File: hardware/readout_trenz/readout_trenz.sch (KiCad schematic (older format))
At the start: 1 part, among them J1 Conn_02x05_Odd_Even

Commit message: Layout Started
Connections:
- net labels removed: 1v8_GPIO1, 1v8_GPIO2, 1v8_GPIO3, 1v8_GPIO4, 3v3_GPIO1, 3v3_GPIO2, 3v3_GPIO3, 3v3_GPIO4, LVDS_GPIO_n1, LVDS_GPIO_n2, LVDS_GPIO_p1, LVDS_GPIO_p2
- wire segments 35 -> 23
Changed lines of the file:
@@
 Text Label 2550 4500 0    50   ~ 0
 B2_[0..31]
-Text Label 11550 5250 0    50   ~ 0
-LVDS_GPIO_n2
-Wire Wire Line
-	12100 5150 11550 5150
-Wire Wire Line
-	11550 5250 12100 5250
-Wire Wire Line
-	12100 4650 11650 4650
-Wire Wire Line
-	11650 4550 12100 4550
-Text Label 11650 4650 0    50   ~ 0
-3v3_GPIO2
-Text Label 11650 4550 0    50   ~ 0
-3v3_GPIO1
-Wire Wire Line
-	12100 4850 11650 4850
-Wire Wire Line
-	11650 4750 12100 4750
-Text Label 11650 4850 0    50   ~ 0
-3v3_GPIO4
-Text Label 11650 4750 0    50   ~ 0
-3v3_GPIO3
-Text Label 11550 5150 0    50   ~ 0
-LVDS_GPIO_p2
-Wire Wire Line
-	11550 5050 12100 5050
-Wire Wire Line
-	12100 4950 11550 4950
-Text Label 11550 5050 0    50   ~ 0
-LVDS_GPIO_n1
-Text Label 11550 4950 0    50   ~ 0
-LVDS_GPIO_p1
-Wire Wire Line
-	12100 4250 11650 4250
-Wire Wire Line
-	11650 4150 12100 4150
-Text Label 11650 4250 0    50   ~ 0
-1v8_GPIO2
-Text Label 11650 4150 0    50   ~ 0
-1v8_GPIO1
-Wire Wire Line
-	12100 4450 11650 4450
-Wire Wire Line
-	11650 4350 12100 4350
-Text Label 11650 4450 0    50   ~ 0
-1v8_GPIO4
-Text Label 11650 4350 0    50   ~ 0
-1v8_GPIO3
 Wire Wire Line
 	2500 6000 3500 6000

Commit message: Radout Layout in progress
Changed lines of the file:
@@
 Wire Bus Line
 	5500 2750 4500 2750
-Text Label 4600 2750 0    50   ~ 0
-Serial_ctrl[0..8]ONE
 Wire Bus Line
 	4500 5750 5500 5750
-Text Label 4650 5750 0    50   ~ 0
-Serial_ctrl[0..8]TWO
 $Sheet
 S 3500 1000 1000 2500

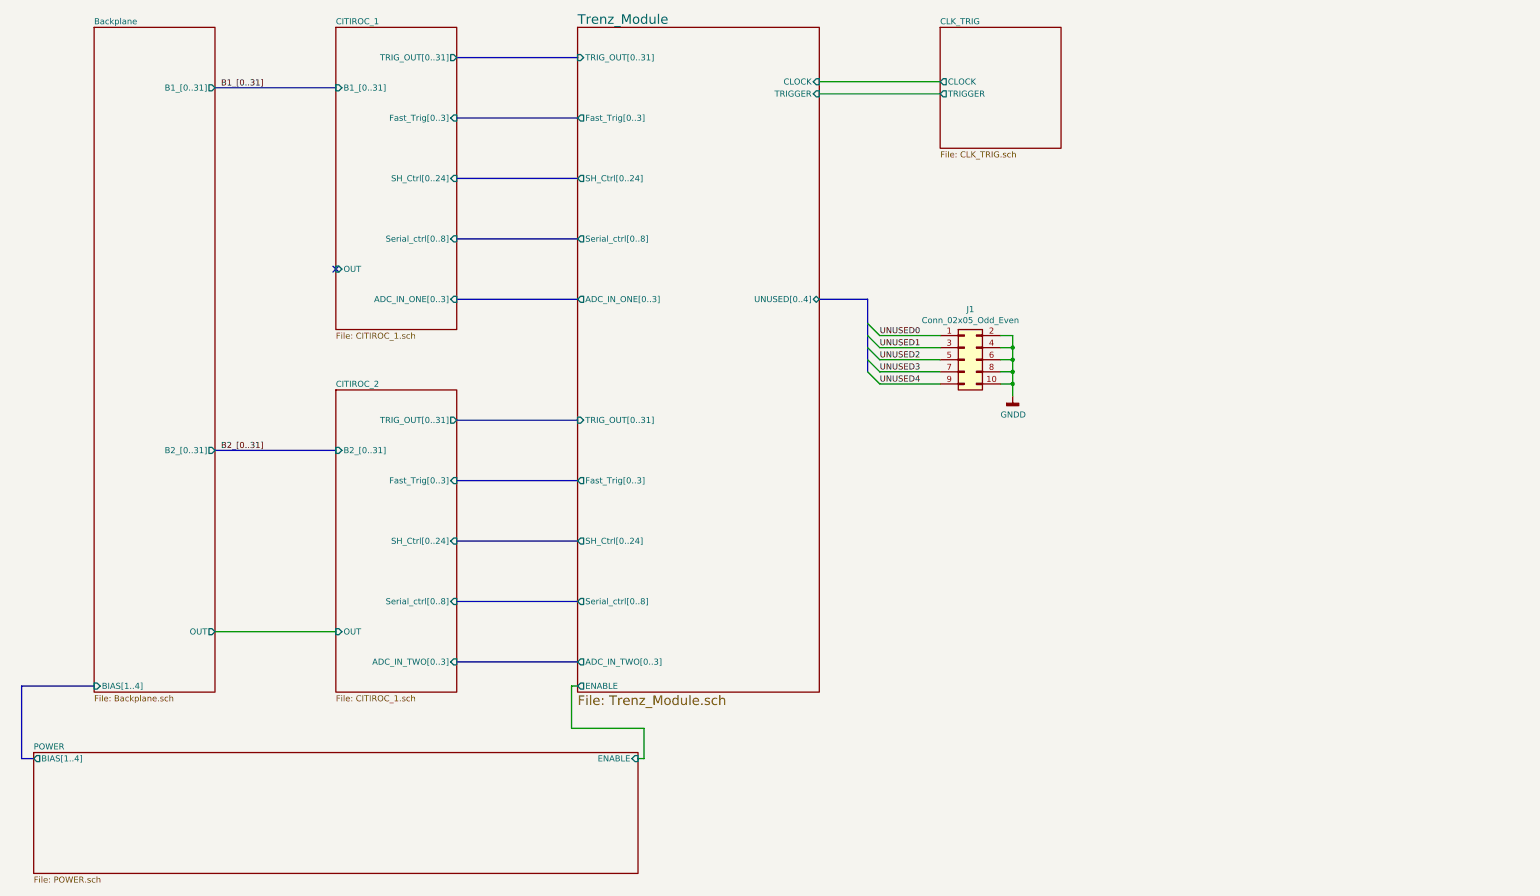
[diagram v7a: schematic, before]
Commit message: Netlist errors fixed
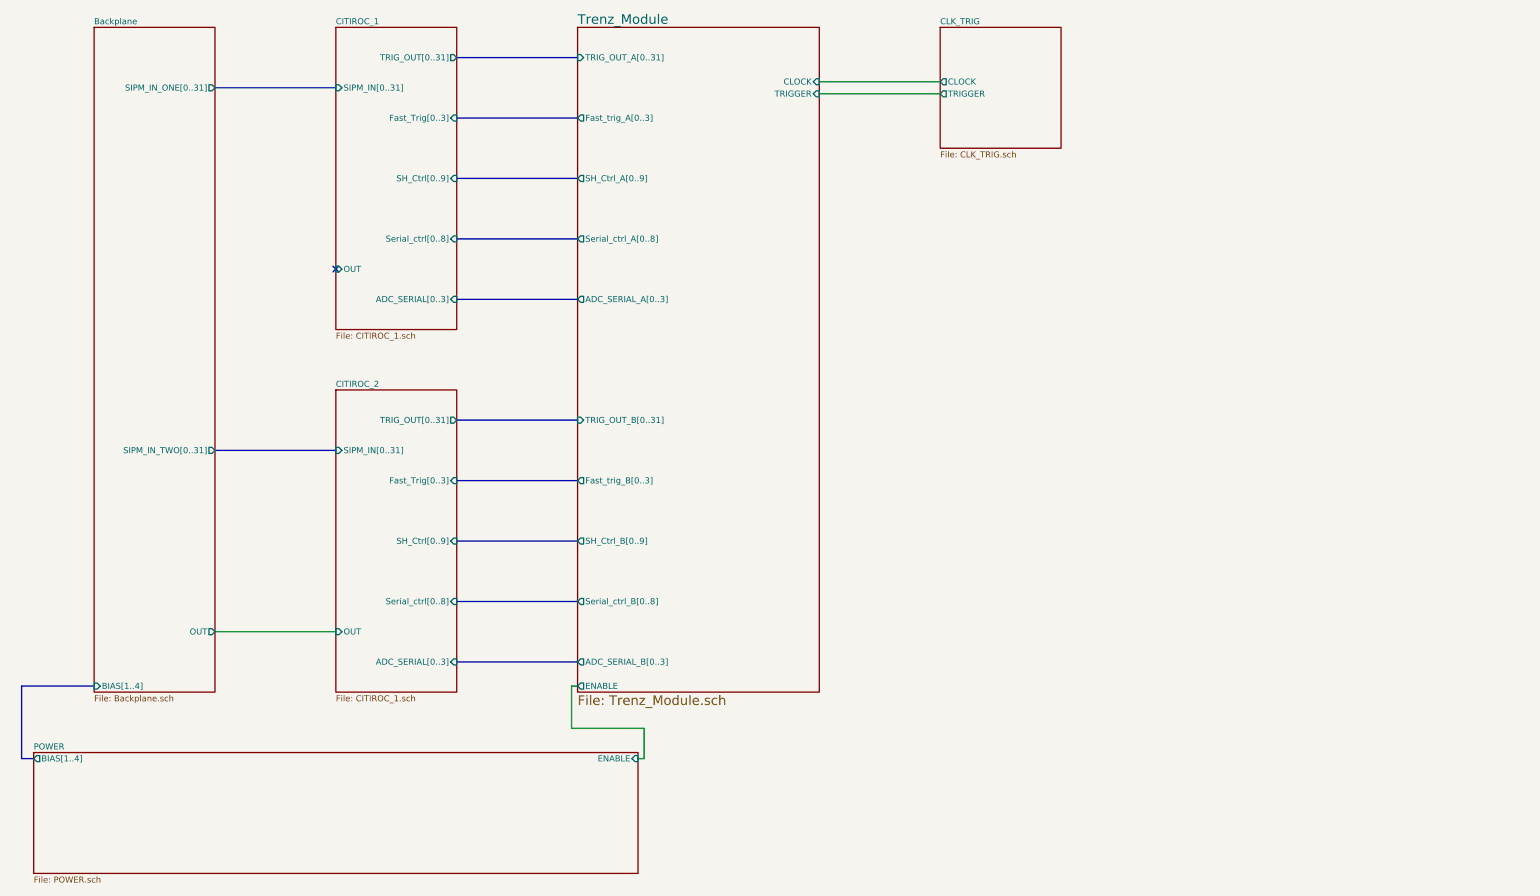
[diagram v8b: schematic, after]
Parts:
- removed J1: Conn_02x05_Odd_Even, Connector_PinHeader_2.54mm:PinHeader_2x05_P2.54mm_Vertical_SMD, symbol Connector_Generic:Conn_02x05_Odd_Even
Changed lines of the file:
@@
 Wire Bus Line
 	2500 4500 3500 4500
-Text Label 2550 4500 0    50   ~ 0
-B2_[0..31]
 Wire Wire Line
 	2500 6000 3500 6000
@@
 F0 "CITIROC_2" 50
 F1 "CITIROC_1.sch" 50
-F2 "B2_[0..31]" I L 3500 4500 50
+F2 "SIPM_IN[0..31]" I L 3500 4500 50
 F3 "OUT" I L 3500 6000 50
 F4 "TRIG_OUT[0..31]" O R 4500 4250 50
-F5 "ADC_IN_TWO[0..3]" I R 4500 6250 50
-F6 "SH_Ctrl[0..24]" I R 4500 5250 50
+F5 "ADC_SERIAL[0..3]" I R 4500 6250 50
+F6 "SH_Ctrl[0..9]" I R 4500 5250 50
 F7 "Serial_ctrl[0..8]" I R 4500 5750 50
 F8 "Fast_Trig[0..3]" I R 4500 4750 50
 $EndSheet
-Text Label 2550 1500 0    50   ~ 0
-B1_[0..31]
 $Sheet
 S 1500 1000 1000 5500
@@
 F0 "Backplane" 50
 F1 "Backplane.sch" 50
-F2 "B2_[0..31]" O R 2500 4500 50
-F3 "OUT" O R 2500 6000 50
-F4 "B1_[0..31]" O R 2500 1500 50
-F5 "BIAS[1..4]" I L 1500 6450 50
+F2 "OUT" O R 2500 6000 50
+F3 "BIAS[1..4]" I L 1500 6450 50
+F4 "SIPM_IN_ONE[0..31]" O R 2500 1500 50
+F5 "SIPM_IN_TWO[0..31]" O R 2500 4500 50
 $EndSheet
 NoConn ~ 3500 3000
@@
 F0 "Trenz_Module" 79
 F1 "Trenz_Module.sch" 79
-F2 "TRIG_OUT[0..31]" I L 5500 1250 50
-F3 "TRIG_OUT[0..31]" I L 5500 4250 50
-F4 "ADC_IN_ONE[0..3]" O L 5500 3250 50
-F5 "ADC_IN_TWO[0..3]" O L 5500 6250 50
-F6 "SH_Ctrl[0..24]" O L 5500 2250 50
-F7 "SH_Ctrl[0..24]" O L 5500 5250 50
-F8 "CLOCK" I R 7500 1450 50
-F9 "TRIGGER" I R 7500 1550 50
-F10 "ENABLE" O L 5500 6450 50
-F11 "Serial_ctrl[0..8]" O L 5500 2750 50
-F12 "Serial_ctrl[0..8]" O L 5500 5750 50
-F13 "Fast_Trig[0..3]" O L 5500 1750 50
-F14 "Fast_Trig[0..3]" O L 5500 4750 50
-F15 "UNUSED[0..4]" B R 7500 3250 50
+F2 "CLOCK" I R 7500 1450 50
+F3 "TRIGGER" I R 7500 1550 50
+F4 "ENABLE" O L 5500 6450 50
+F5 "TRIG_OUT_A[0..31]" I L 5500 1250 50
+F6 "TRIG_OUT_B[0..31]" I L 5500 4250 50
+F7 "SH_Ctrl_B[0..9]" O L 5500 5250 50
+F8 "Fast_trig_B[0..3]" O L 5500 4750 50
+F9 "ADC_SERIAL_B[0..3]" O L 5500 6250 50
+F10 "SH_Ctrl_A[0..9]" O L 5500 2250 50
+F11 "ADC_SERIAL_A[0..3]" O L 5500 3250 50
+F12 "Serial_ctrl_B[0..8]" O L 5500 5750 50
+F13 "Serial_ctrl_A[0..8]" O L 5500 2750 50
+F14 "Fast_trig_A[0..3]" O L 5500 1750 50
 $EndSheet
 Wire Wire Line
@@
 F0 "CITIROC_1" 50
 F1 "CITIROC_1.sch" 50
-F2 "B1_[0..31]" I L 3500 1500 50
+F2 "SIPM_IN[0..31]" I L 3500 1500 50
 F3 "TRIG_OUT[0..31]" O R 4500 1250 50
-F4 "ADC_IN_ONE[0..3]" I R 4500 3250 50
-F5 "SH_Ctrl[0..24]" I R 4500 2250 50
+F4 "ADC_SERIAL[0..3]" I R 4500 3250 50
+F5 "SH_Ctrl[0..9]" I R 4500 2250 50
 F6 "OUT" I L 3500 3000 50
 F7 "Serial_ctrl[0..8]" I R 4500 2750 50
@@
 Wire Bus Line
 	5500 4750 4500 4750
-$Comp
-L Connector_Generic:Conn_02x05_Odd_Even J1
-U 1 1 60DDF7C6
-P 8700 3750
-F 0 "J1" H 8750 4167 50  0000 C CNN
-F 1 "Conn_02x05_Odd_Even" H 8750 4076 50  0000 C CNN
-F 2 "Connector_PinHeader_2.54mm:PinHeader_2x05_P2.54mm_Vertical_SMD" H 8700 3750 50  0001 C CNN
-F 3 "~" H 8700 3750 50  0001 C CNN
-	1    8700 3750
-	1    0    0    -1
-$EndComp
-Wire Wire Line
-	9000 3550 9100 3550
-Wire Wire Line
-	9100 3550 9100 3650
-Wire Wire Line
-	9000 3650 9100 3650
-Connection ~ 9100 3650
-Wire Wire Line
-	9100 3650 9100 3750
-Wire Wire Line
-	9000 3750 9100 3750
-Connection ~ 9100 3750
-Wire Wire Line
-	9100 3750 9100 3850
-Wire Wire Line
-	9000 3850 9100 3850
-Connection ~ 9100 3850
-Wire Wire Line
-	9100 3850 9100 3950
-Wire Wire Line
-	9000 3950 9100 3950
-Connection ~ 9100 3950
-Wire Wire Line
-	9100 3950 9100 4050
-$Comp
-L power:GNDD #PWR01
-U 1 1 60DE3614
-P 9100 4050
-F 0 "#PWR01" H 9100 3800 50  0001 C CNN
-F 1 "GNDD" H 9104 3895 50  0000 C CNN
-F 2 "" H 9100 4050 50  0001 C CNN
-F 3 "" H 9100 4050 50  0001 C CNN
-	1    9100 4050
-	1    0    0    -1
-$EndComp
-Text Label 8000 3550 0    50   ~ 0
-UNUSED0
-Text Label 8000 3650 0    50   ~ 0
-UNUSED1
-Text Label 8000 3750 0    50   ~ 0
-UNUSED2
-Text Label 8000 3850 0    50   ~ 0
-UNUSED3
-Text Label 8000 3950 0    50   ~ 0
-UNUSED4
-Wire Wire Line
-	8500 3550 8000 3550
-Wire Wire Line
-	8500 3650 8000 3650
-Wire Wire Line
-	8500 3750 8000 3750
-Wire Wire Line
-	8500 3850 8000 3850
-Wire Wire Line
-	8500 3950 8000 3950
-Entry Wire Line
-	7900 3450 8000 3550
-Entry Wire Line
-	7900 3550 8000 3650
-Entry Wire Line
-	7900 3650 8000 3750
-Entry Wire Line
-	7900 3750 8000 3850
-Entry Wire Line
-	7900 3850 8000 3950
-Wire Bus Line
-	7900 3250 7500 3250
-Wire Bus Line
-	7900 3250 7900 3850
 $EndSCHEMATC
